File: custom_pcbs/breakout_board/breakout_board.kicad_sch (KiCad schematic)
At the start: 2 parts, among them J1 INPUT_FROM_PI, J2 PMW3901_OUT

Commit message: Basic pcb version
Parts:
- added H1, H2, H3, H4: MountingHole, MountingHole:MountingHole_2.2mm_M2, symbol Mechanical:MountingHole
- J1: footprint (none) -> Connector_PinHeader_2.54mm:PinHeader_1x10_P2.54mm_Vertical
- J2: footprint (none) -> Connector_PinHeader_2.54mm:PinHeader_1x09_P2.54mm_Vertical
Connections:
- net SPI_MISO: now reaches J1.4 (Pin_4)
- net SPI_MISO: now also J2.5 (Pin_5)
- net SPI_CLK: now reaches J1.5 (Pin_5)
- net SPI_CLK: now also J2.4 (Pin_4)
- net SPI_CS: now reaches J1.6 (Pin_6)
- net SPI_CS: now also J2.6 (Pin_6)

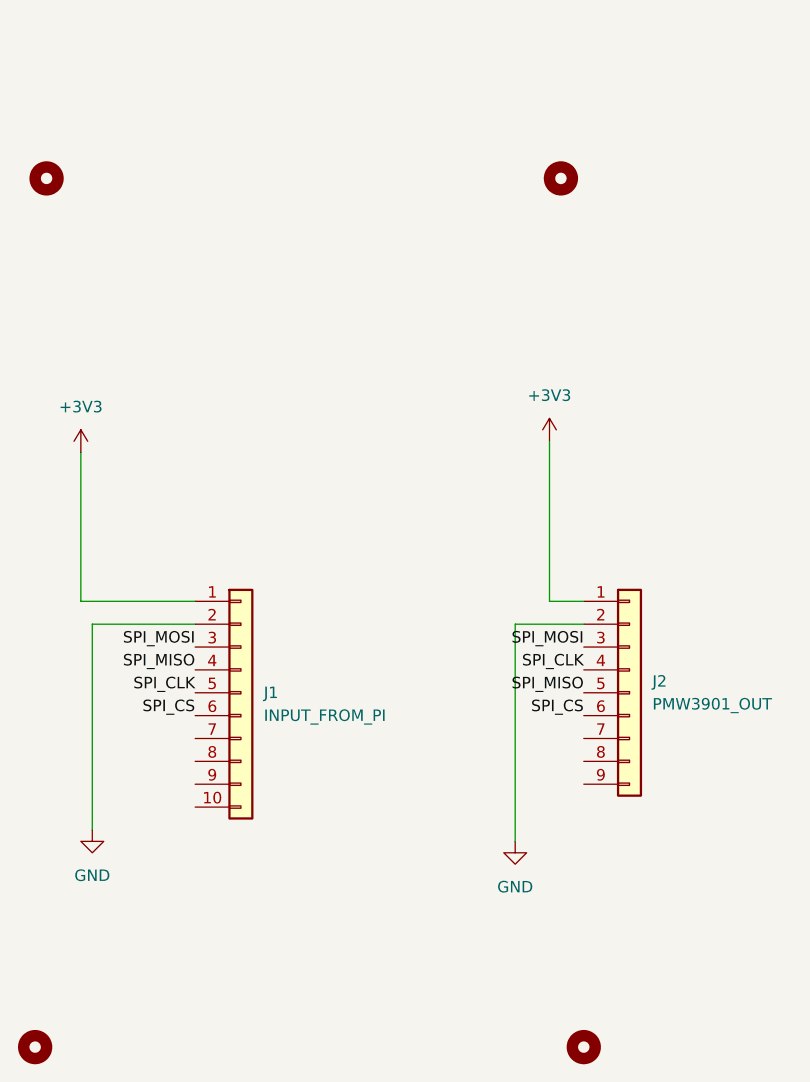
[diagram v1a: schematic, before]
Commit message: Added more sensors
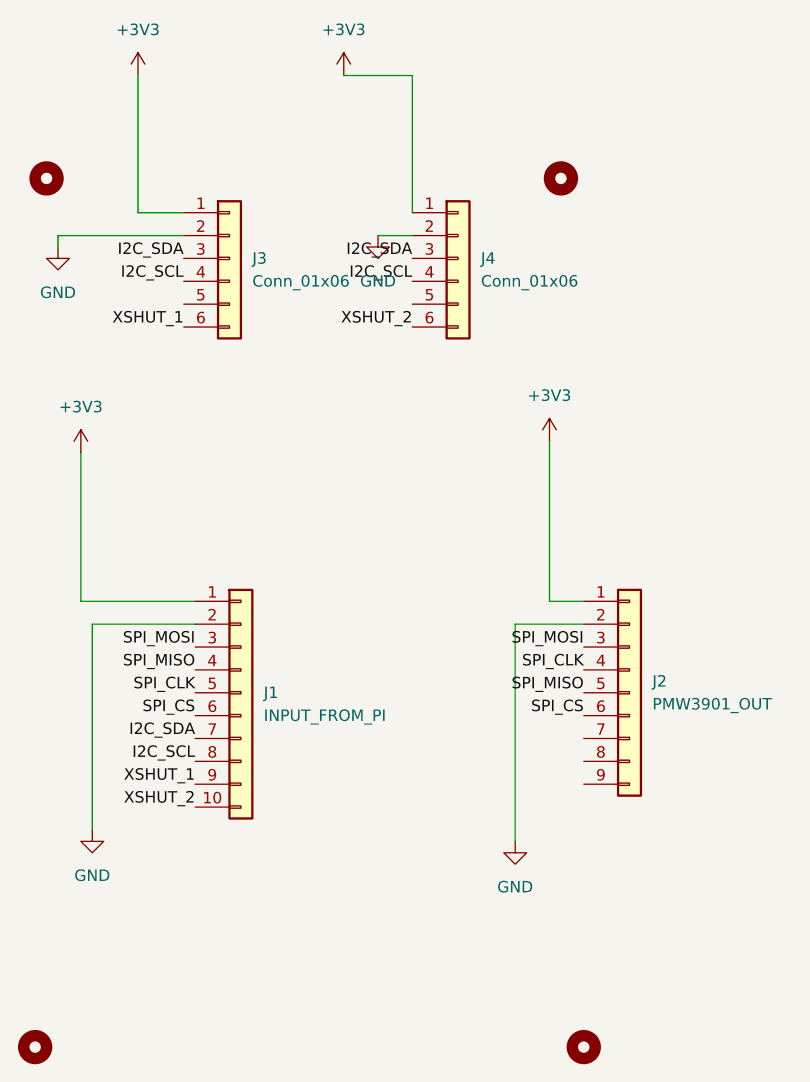
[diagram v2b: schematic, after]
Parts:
- added J3, J4: Conn_01x06, Connector_PinHeader_2.54mm:PinHeader_1x06_P2.54mm_Vertical, symbol Connector_Generic:Conn_01x06
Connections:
- net +3V3: now also J3.1 (Pin_1), J4.1 (Pin_1)
- net GND: now also J3.2 (Pin_2), J4.2 (Pin_2)
- net XSHUT_2: now reaches J1.10 (Pin_10)
- net XSHUT_2: now also J4.6 (Pin_6)
- net I2C_SDA: now reaches J1.7 (Pin_7)
- net I2C_SDA: now also J3.3 (Pin_3), J4.3 (Pin_3)
- net I2C_SCL: now reaches J1.8 (Pin_8)
- net I2C_SCL: now also J3.4 (Pin_4), J4.4 (Pin_4)
- net XSHUT_1: now reaches J1.9 (Pin_9)
- net XSHUT_1: now also J3.6 (Pin_6)
